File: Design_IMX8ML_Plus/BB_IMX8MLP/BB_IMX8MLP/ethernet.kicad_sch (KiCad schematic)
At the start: 26 parts, among them J5 RJ45_JK0654219, J6 RJ45_JK0654219, U1 KSZ9131RNXI, Y2 25MHz

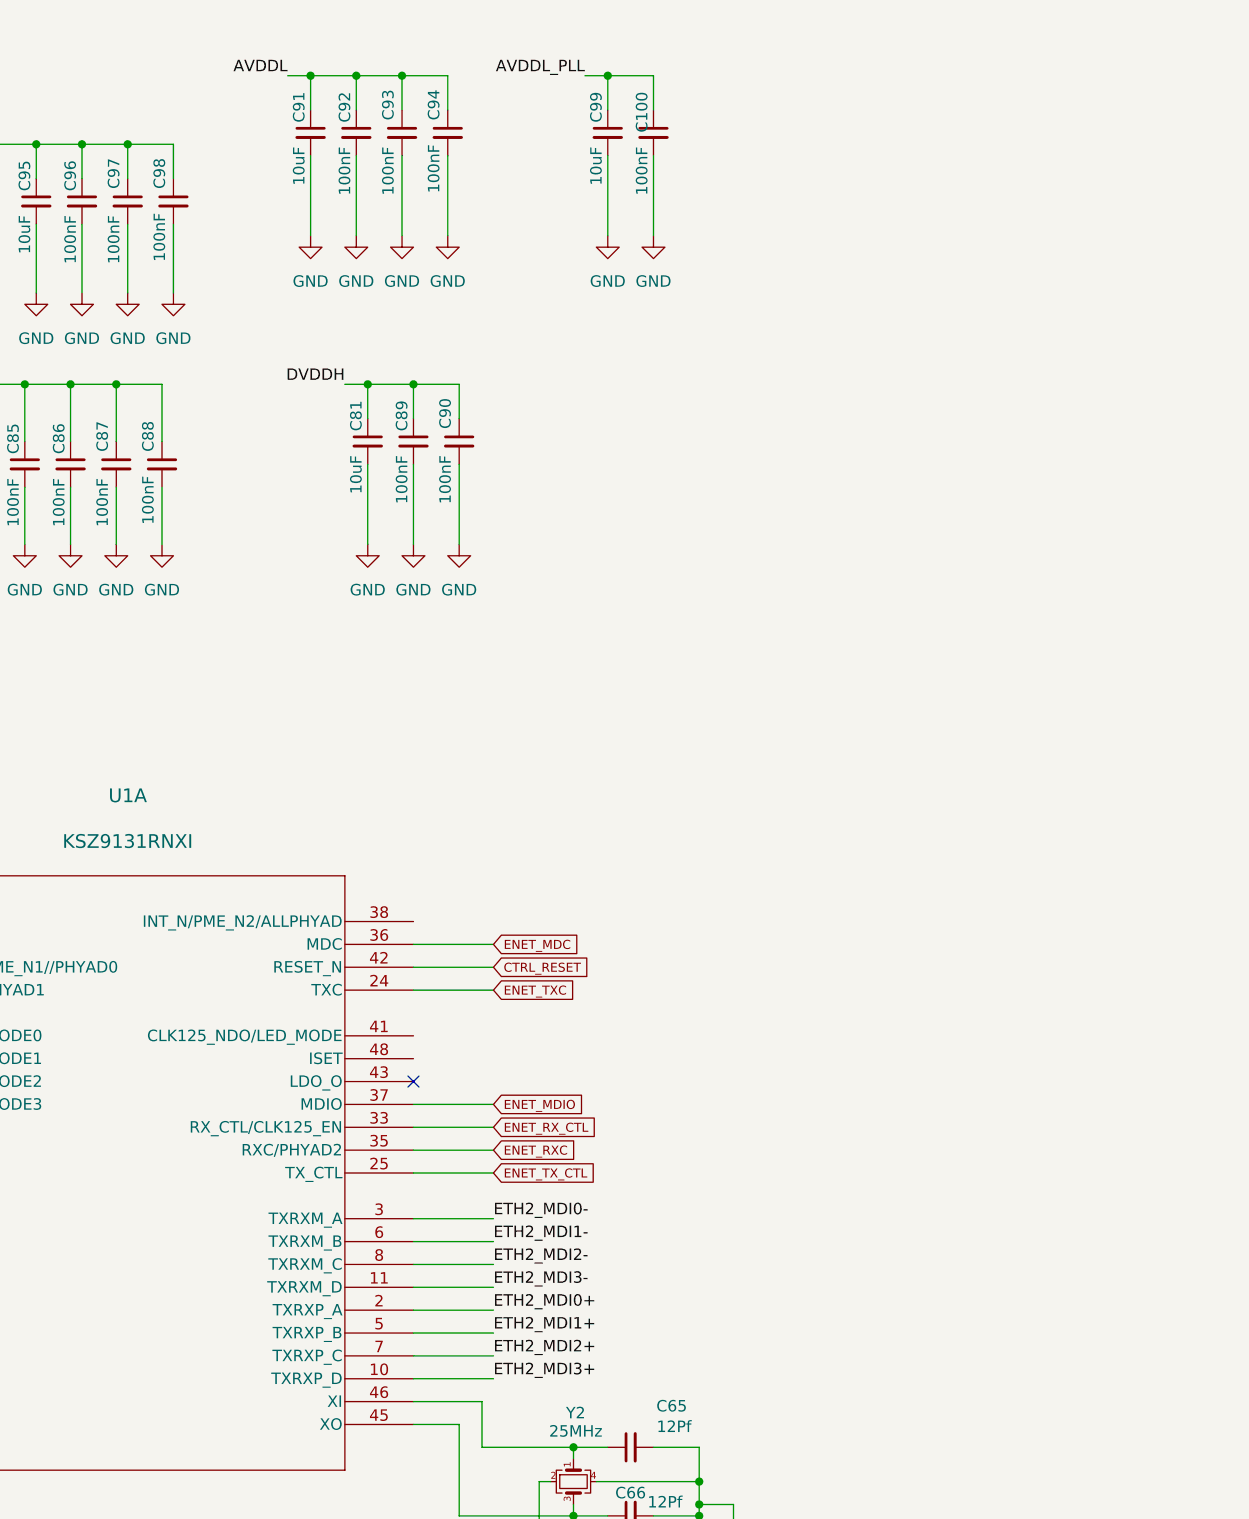
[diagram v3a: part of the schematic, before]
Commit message: Add LVDs and CSI Interface
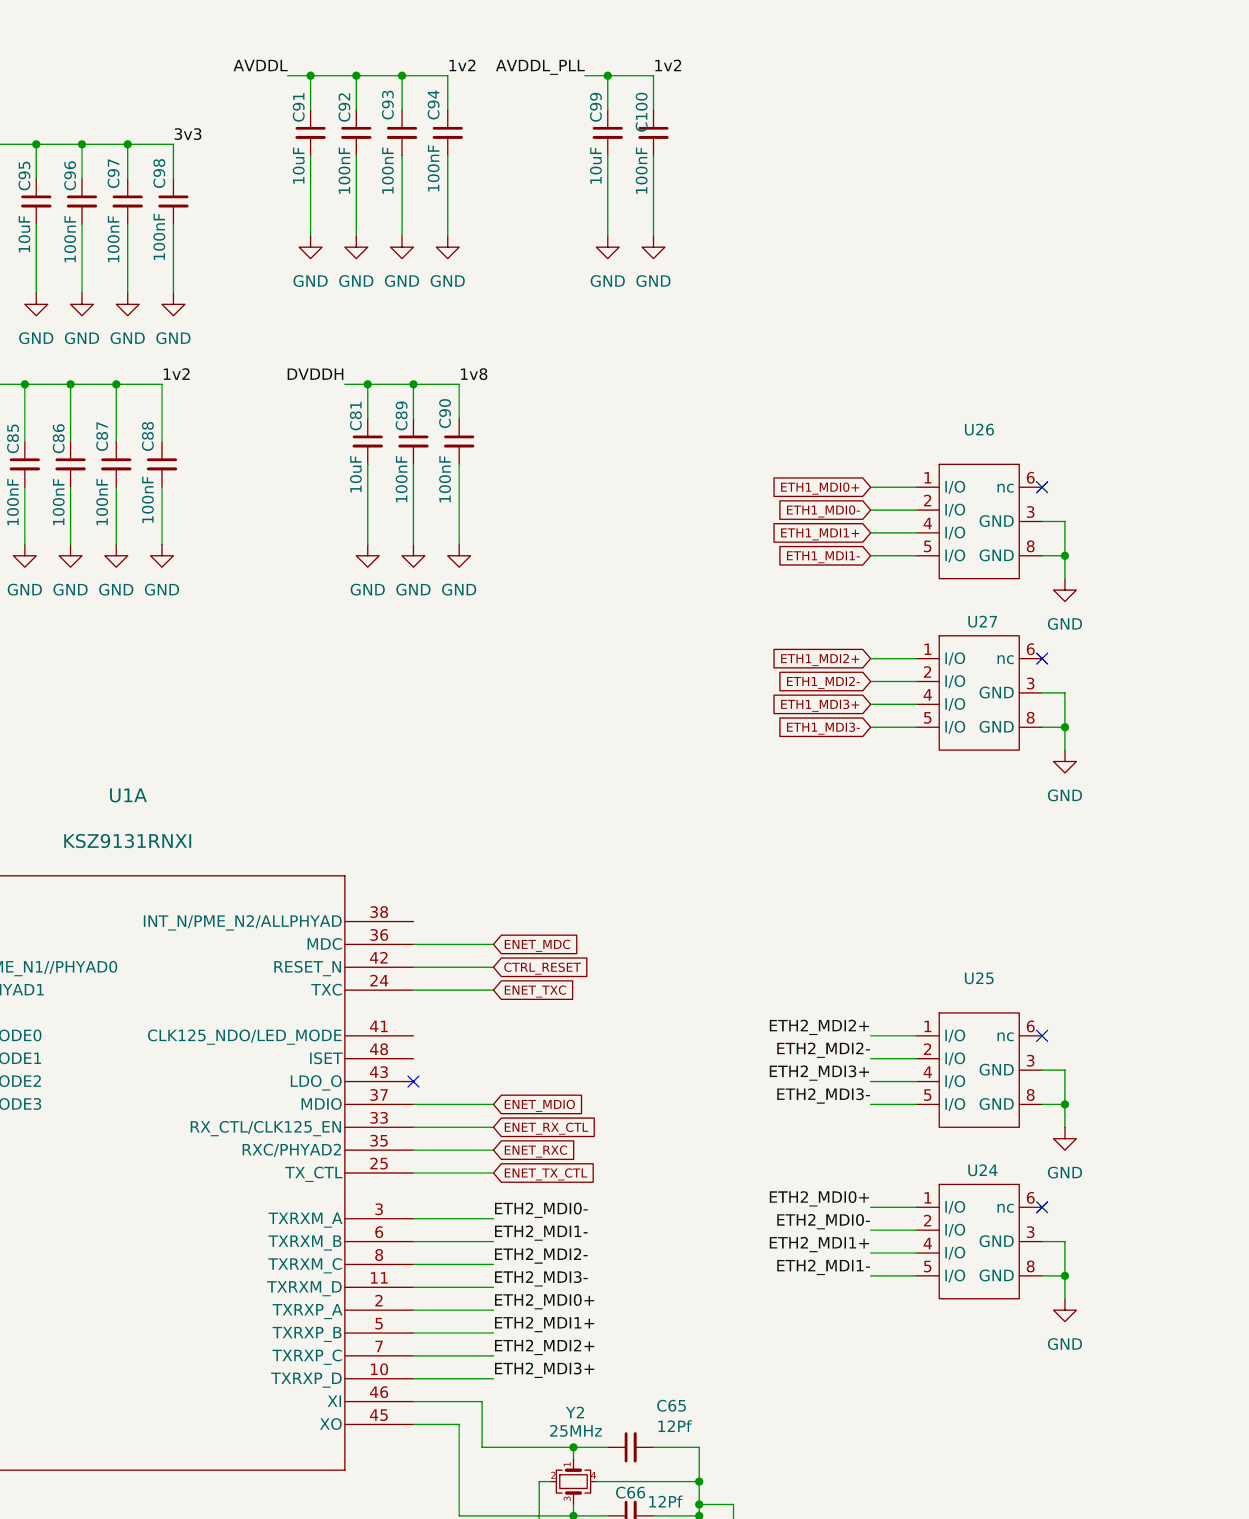
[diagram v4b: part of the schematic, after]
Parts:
- added U24, U25, U26, U27: ~, _W_SBC:DFN10_U-DFN2510-10_DIO, symbol _W_MX8M:D3V3F4U10LP-7
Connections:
- net AVDDL is gone; now on net 1v2: C91.1, C92.1, C93.1, C94.1, U1.4 (AVDDL), U1.9 (AVDDL)
- net AVDDL_PLL is gone; now on net 1v2: C100.1, C99.1, U1.44 (AVDDL_PLL)
- net ETH1_MDI0+: now also U26.1 (I/O)
- net ETH1_MDI0-: now also U26.2 (I/O)
- net ETH1_MDI1+: now also U26.4 (I/O)
- net ETH1_MDI1-: now also U26.5 (I/O)
- net ETH1_MDI2+: now also U27.1 (I/O)
- net ETH1_MDI2-: now also U27.2 (I/O)
- net ETH1_MDI3+: now also U27.4 (I/O)
- net ETH1_MDI3-: now also U27.5 (I/O)
- net ETH2_MDI0+: now also U24.1 (I/O)
- net ETH2_MDI0-: now also U24.2 (I/O)
- net ETH2_MDI1+: now also U24.4 (I/O)
- net ETH2_MDI1-: now also U24.5 (I/O)
- net ETH2_MDI2+: now also U25.1 (I/O)
- net ETH2_MDI2-: now also U25.2 (I/O)
- net ETH2_MDI3+: now also U25.4 (I/O)
- net ETH2_MDI3-: now also U25.5 (I/O)
- net GND: now also U24.3 (GND), U24.8 (GND), U25.3 (GND), U25.8 (GND), U26.3 (GND), U26.8 (GND), U27.3 (GND), U27.8 (GND)
- net 3v3: now reaches C95.1, C96.1, C97.1, C98.1, U1.1 (AVDDH), U1.12 (AVDDH)
- net 1v2: now reaches C82.1, C83.1, C84.1, C85.1, C86.1, C87.1, C88.1, U1.18 (DVDDL), U1.23 (DVDDL), U1.26 (DVDDL), U1.30 (DVDDL), U1.39 (DVDDL)
- net DVDDH renamed 1v8
- new net: U26.10 (nc), U26.6 (nc), U26.7 (nc), U26.9 (nc)
- new net: U25.10 (nc), U25.6 (nc), U25.7 (nc), U25.9 (nc)
- new net: U24.10 (nc), U24.6 (nc), U24.7 (nc), U24.9 (nc)
- new net: U27.10 (nc), U27.6 (nc), U27.7 (nc), U27.9 (nc)
- no-connect marks 1 -> 5

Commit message: Review
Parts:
- added C142, C143, C144, C145, C146, C147, C148, C149: 100nF, Capacitor_SMD:C_0402_1005Metric, symbol Device:C_Small
- added R47: 10K, Resistor_SMD:R_0402_1005Metric, symbol Device:R_Small
- added R58: 6.04k, Resistor_SMD:R_0402_1005Metric, symbol Device:R_Small
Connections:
- net 1v8: now also R47.1
- net 3v3: now also J5.14 (LED2+), J5.16 (LED1+), J6.14 (LED2+), J6.16 (LED1+)
- net GND: now also C142.2, C143.2, C144.2, C145.2, C146.2, C147.2, C148.2, C149.2, R58.1
- net at J6.1 (MXCT3): now also C148.1
- net at J6.12 (MXCT1): now also C146.1
- net at J6.6 (MXCT2): now also C147.1
- net at J6.7 (MXCT4): now also C149.1
- net at J5.1 (MXCT3): now also C144.1
- net at J5.12 (MXCT1): now also C142.1
- net at J5.6 (MXCT2): now also C143.1
- net at J5.7 (MXCT4): now also C145.1
- net LED_MODE: now reaches U1.41 (CLK125_NDO/LED_MODE)
- net LED_MODE: now also R47.2
- net ISET: now reaches U1.48 (ISET)
- net ISET: now also R58.2
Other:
- moved on the sheet: U24, U25, U26, U27

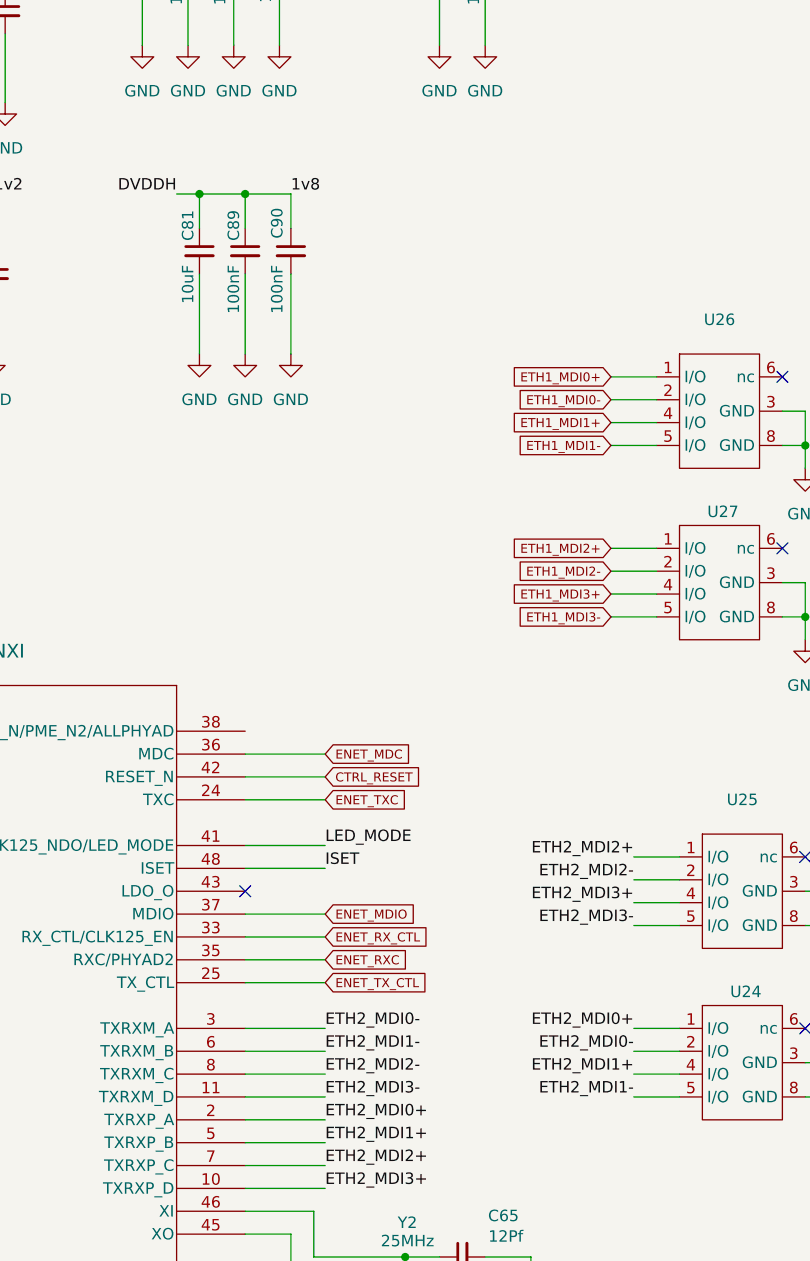
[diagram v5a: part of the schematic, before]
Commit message: reorganization of the componentes
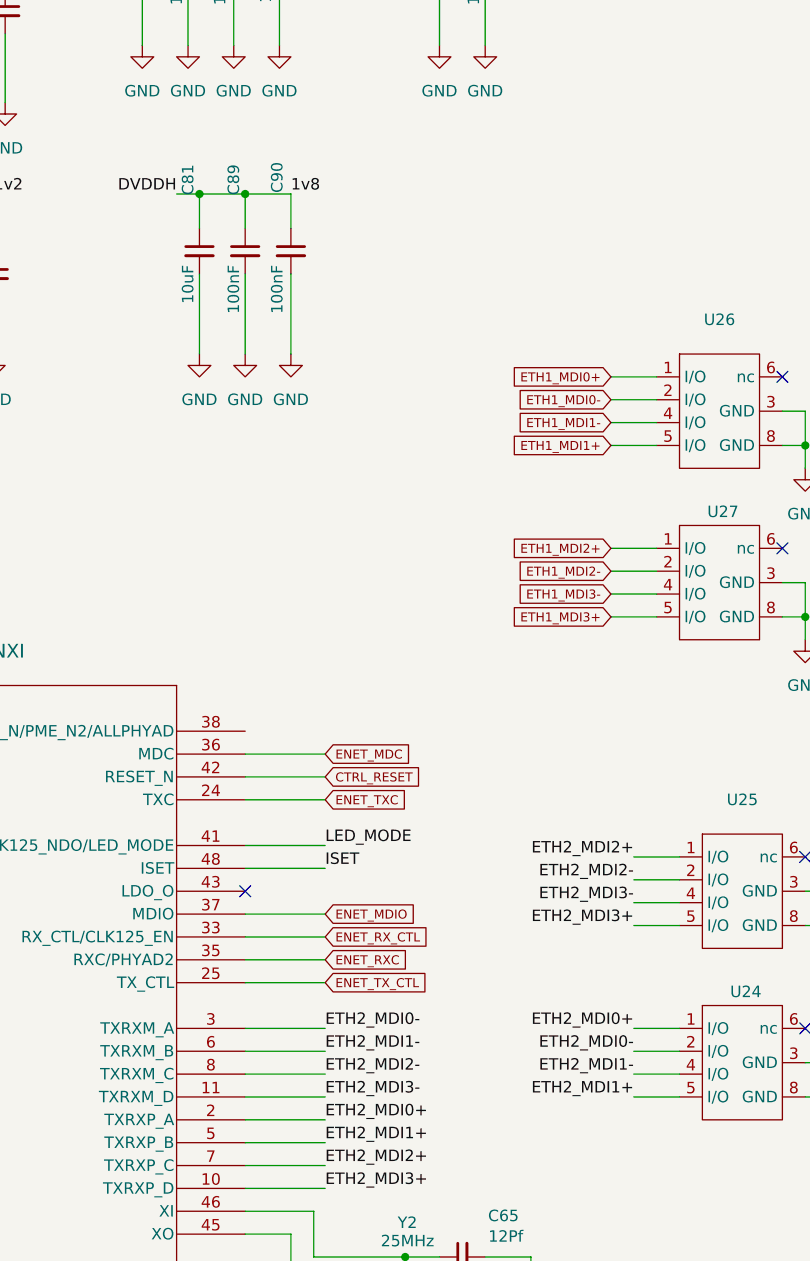
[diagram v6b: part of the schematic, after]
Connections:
- net ETH1_MDI1+: now also U26.5 (I/O); no longer U26.4 (I/O)
- net ETH1_MDI1-: now also U26.4 (I/O); no longer U26.5 (I/O)
- net ETH1_MDI3+: now also U27.5 (I/O); no longer U27.4 (I/O)
- net ETH1_MDI3-: now also U27.4 (I/O); no longer U27.5 (I/O)
- net ETH2_MDI1+: now also U24.5 (I/O); no longer U24.4 (I/O)
- net ETH2_MDI1-: now also U24.4 (I/O); no longer U24.5 (I/O)
- net ETH2_MDI3+: now also U25.5 (I/O); no longer U25.4 (I/O)
- net ETH2_MDI3-: now also U25.4 (I/O); no longer U25.5 (I/O)
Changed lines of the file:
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@@
 	(wire
 		(pts
-			(xy 152.4 137.16) (xy 157.48 137.16)
+			(xy 152.4 134.62) (xy 157.48 134.62)
 		)
 		(stroke
@@
 	(wire
 		(pts
-			(xy 104.14 55.88) (xy 104.14 59.69)
-		)
-		(stroke
-			(width 0)
-			(type default)
-		)
-	)
-	(wire
-		(pts
 			(xy 171.45 152.4) (xy 173.99 152.4)
 		)
@@
 	(wire
 		(pts
-			(xy 152.4 153.67) (xy 157.48 153.67)
+			(xy 152.4 156.21) (xy 157.48 156.21)
 		)
 		(stroke
@@
 	(wire
 		(pts
-			(xy 149.86 81.28) (xy 154.94 81.28)
+			(xy 149.86 83.82) (xy 154.94 83.82)
 		)
 		(stroke
@@
 	(wire
 		(pts
-			(xy 152.4 134.62) (xy 157.48 134.62)
+			(xy 152.4 137.16) (xy 157.48 137.16)
 		)
 		(stroke
@@
 	(wire
 		(pts
+			(xy 109.22 55.88) (xy 109.22 59.69)
+		)
+		(stroke
+			(width 0)
+			(type default)
+		)
+	)
+	(wire
+		(pts
 			(xy 127 180.34) (xy 127 181.61)
 		)
@@
 	(wire
 		(pts
-			(xy 149.86 100.33) (xy 154.94 100.33)
+			(xy 149.86 102.87) (xy 154.94 102.87)
 		)
 		(stroke
@@
 	(wire
 		(pts
-			(xy 149.86 83.82) (xy 154.94 83.82)
+			(xy 149.86 81.28) (xy 154.94 81.28)
 		)
 		(stroke
@@
 	(wire
 		(pts
-			(xy 149.86 102.87) (xy 154.94 102.87)
+			(xy 149.86 100.33) (xy 154.94 100.33)
 		)
 		(stroke
@@
 	(wire
 		(pts
-			(xy 109.22 59.69) (xy 109.22 55.88)
+			(xy 104.14 55.88) (xy 104.14 59.69)
 		)
 		(stroke
@@
 	(wire
 		(pts
-			(xy 114.3 55.88) (xy 114.3 59.69)
-		)
-		(stroke
-			(width 0)
-			(type default)
-		)
-	)
-	(wire
-		(pts
 			(xy 222.25 134.62) (xy 222.25 148.59)
 		)
@@
 	(wire
 		(pts
-			(xy 152.4 156.21) (xy 157.48 156.21)
+			(xy 152.4 153.67) (xy 157.48 153.67)
 		)
 		(stroke
@@
 	(wire
 		(pts
+			(xy 114.3 55.88) (xy 114.3 59.69)
+		)
+		(stroke
+			(width 0)
+			(type default)
+		)
+	)
+	(wire
+		(pts
 			(xy 217.17 124.46) (xy 217.17 148.59)
 		)
@@
 	)
 	(label "ETH2_MDI1-"
-		(at 152.4 156.21 180)
+		(at 152.4 153.67 180)
 		(effects
 			(font
@@
 	)
 	(label "ETH2_MDI3+"
-		(at 152.4 134.62 180)
+		(at 152.4 137.16 180)
 		(effects
 			(font
@@
 	)
 	(label "ETH2_MDI1+"
-		(at 152.4 153.67 180)
+		(at 152.4 156.21 180)
 		(effects
 			(font
@@
 	)
 	(label "ETH2_MDI3-"
-		(at 152.4 137.16 180)
+		(at 152.4 134.62 180)
 		(effects
 			(font
@@
 	(global_label "ETH1_MDI3+"
 		(shape input)
-		(at 149.86 100.33 180)
+		(at 149.86 102.87 180)
 		(fields_autoplaced yes)
 		(effects
@@
 		)
 		(property "Intersheetrefs" "${INTERSHEET_REFS}"
-			(at 138.2715 100.33 0)
+			(at 138.2715 102.87 0)
 			(effects
 				(font
@@
 	(global_label "ETH1_MDI1-"
 		(shape input)
-		(at 149.86 83.82 180)
+		(at 149.86 81.28 180)
 		(fields_autoplaced yes)
 		(effects
@@
 		)
 		(property "Intersheetrefs" "${INTERSHEET_REFS}"
-			(at 138.2715 83.82 0)
+			(at 138.2715 81.28 0)
 			(effects
 				(font
@@
 	(global_label "ETH1_MDI3-"
 		(shape input)
-		(at 149.86 102.87 180)
+		(at 149.86 100.33 180)
 		(fields_autoplaced yes)
 		(effects
@@
 		)
 		(property "Intersheetrefs" "${INTERSHEET_REFS}"
-			(at 138.2715 102.87 0)
+			(at 138.2715 100.33 0)
 			(effects
 				(font
@@
 	(global_label "ETH1_MDI1+"
 		(shape input)
-		(at 149.86 81.28 180)
+		(at 149.86 83.82 180)
 		(fields_autoplaced yes)
 		(effects
@@
 		)
 		(property "Intersheetrefs" "${INTERSHEET_REFS}"
-			(at 138.2715 81.28 0)
+			(at 138.2715 83.82 0)
 			(effects
 				(font
@@
 		(dnp no)
 		(property "Reference" "C89"
-			(at 107.95 57.658 90)
+			(at 107.95 52.578 90)
 			(effects
 				(font
@@
 		(dnp no)
 		(property "Reference" "C81"
-			(at 102.87 57.658 90)
+			(at 102.87 52.578 90)
 			(effects
 				(font
@@
 		(dnp no)
 		(property "Reference" "C90"
-			(at 112.776 57.404 90)
+			(at 112.776 52.324 90)
 			(effects
 				(font
